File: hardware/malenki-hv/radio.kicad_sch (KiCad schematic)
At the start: 22 parts, among them U1 A7105, Y1 16mhz Seiko Epson Q24FA20H005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

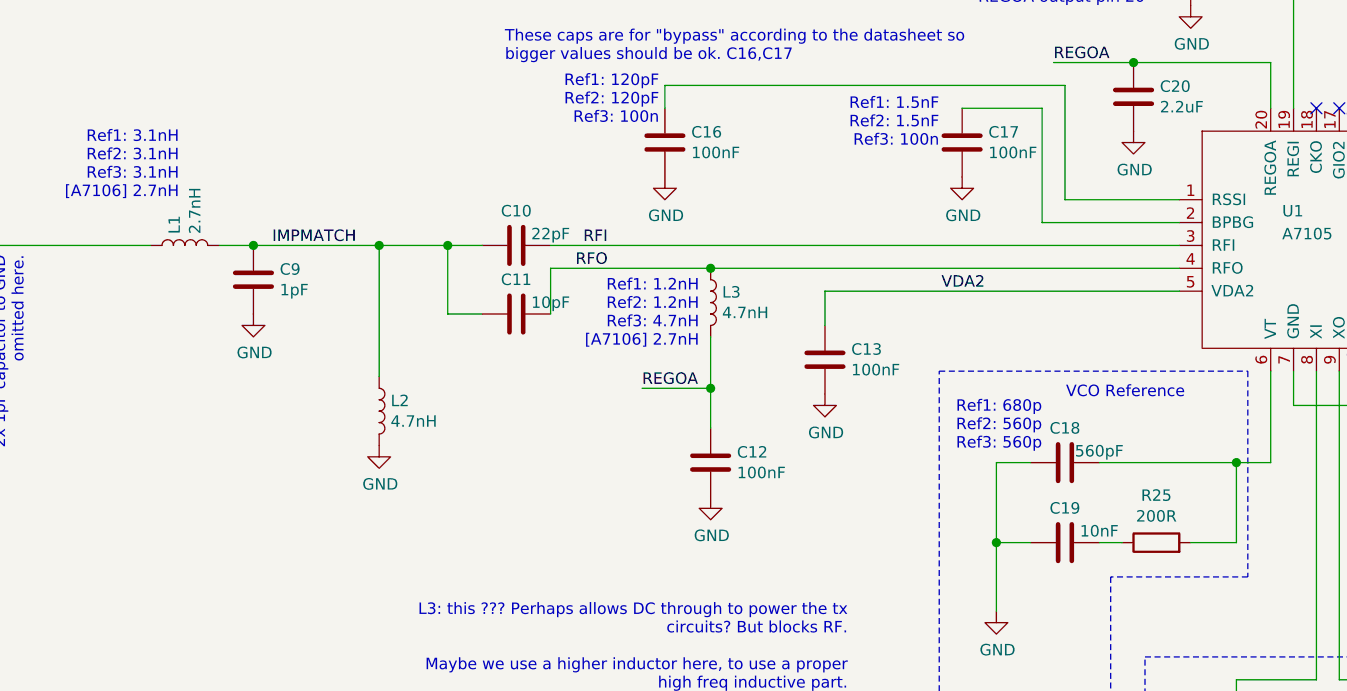
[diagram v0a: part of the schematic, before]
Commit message: Updated u1 QFN symbol by adding solder paste layer, minor schematic updates to fix check errors, converted to kiCad 9, Updated BOM with LSCS numbers, fixed BOM errors.
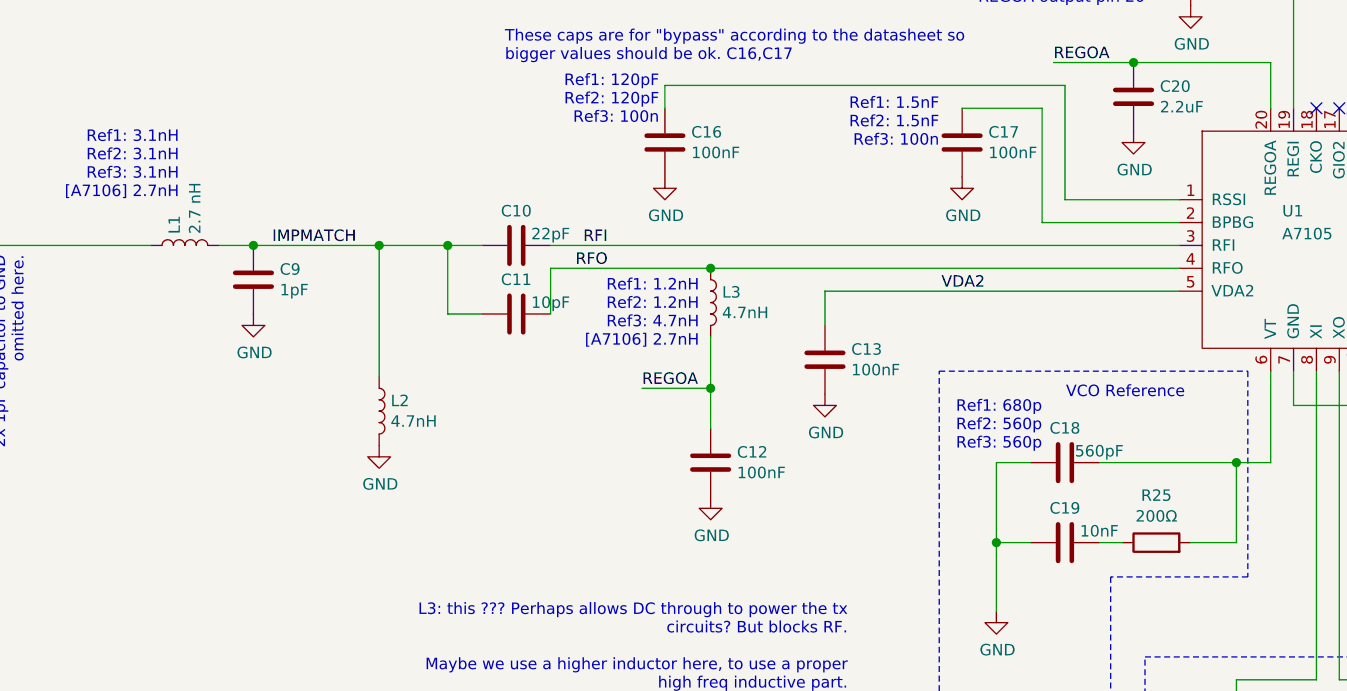
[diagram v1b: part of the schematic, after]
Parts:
- C10, C9: footprint Capacitor_SMD:C_0402_1005Metric_Pad0.74x0.62mm_HandSolder -> Capacitor_SMD:C_0402_1005Metric; Manufacturer Guangdong Fenghua Advanced -> FH
- C11, C14, C15, C19: footprint Capacitor_SMD:C_0402_1005Metric_Pad0.74x0.62mm_HandSolder -> Capacitor_SMD:C_0402_1005Metric
- C12, C13, C16, C17, C22, C23: footprint Capacitor_SMD:C_0402_1005Metric_Pad0.74x0.62mm_HandSolder -> Capacitor_SMD:C_0402_1005Metric; Alternate LCSC PN (none) -> C14663; MPN (none) -> CL05B104KB54PNC
- C18: footprint Capacitor_SMD:C_0402_1005Metric_Pad0.74x0.62mm_HandSolder -> Capacitor_SMD:C_0402_1005Metric; MPN CL05C561JB5NNNC -> 0402B561K500NT; Manufacturer Samsung -> FH
- C20, C21: MPN CL05A225MQ5NSNC -> CL10A225KO8NNNC
- L1: value 2.7nH -> 2.7 nH; footprint Inductor_SMD:L_0402_1005Metric_Pad0.77x0.64mm_HandSolder -> Inductor_SMD:L_0402_1005Metric; MPN (none) -> MLK1005S2N7ST000; Manufacturer Sunlord -> TDK
- L2: footprint Inductor_SMD:L_0402_1005Metric_Pad0.77x0.64mm_HandSolder -> Inductor_SMD:L_0402_1005Metric; Alternate LCSC PN (none) -> C1030
- L3: footprint Inductor_SMD:L_0402_1005Metric_Pad0.77x0.64mm_HandSolder -> Inductor_SMD:L_0402_1005Metric; Alternate LCSC PN (none) -> C1030; MPN VHF160808H4N7ST -> LQW15AN4N7D10D; Manufacturer Guangdong Fenghua -> Murata
- R25: value 200R -> 200Ω; Partnum 10k -> (none)
- Y1: value 16mhz Seiko Epson Q24FA20H0051200 -> 16mhz Seiko Epson Q24FA20H0051200; MPN Q24FA20H0051200 -> Q24FA20H00512; Manufacturer Seiko Epson -> Epson
